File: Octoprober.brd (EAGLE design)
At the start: 130.8 x 91.7 mm, 144 parts, among them J1 10118193-0001LF, J2 26-60-4020, P1 TC33X-2-103E, SW1 101-0134-EV, SW2 EVQ-Q2203W, SW3 EVQ-Q2203W, SW4 EVQ-Q2203W, SW5 EVQ-Q2203W, U1 P8X32A-M44, U10 MAX31855KASA+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

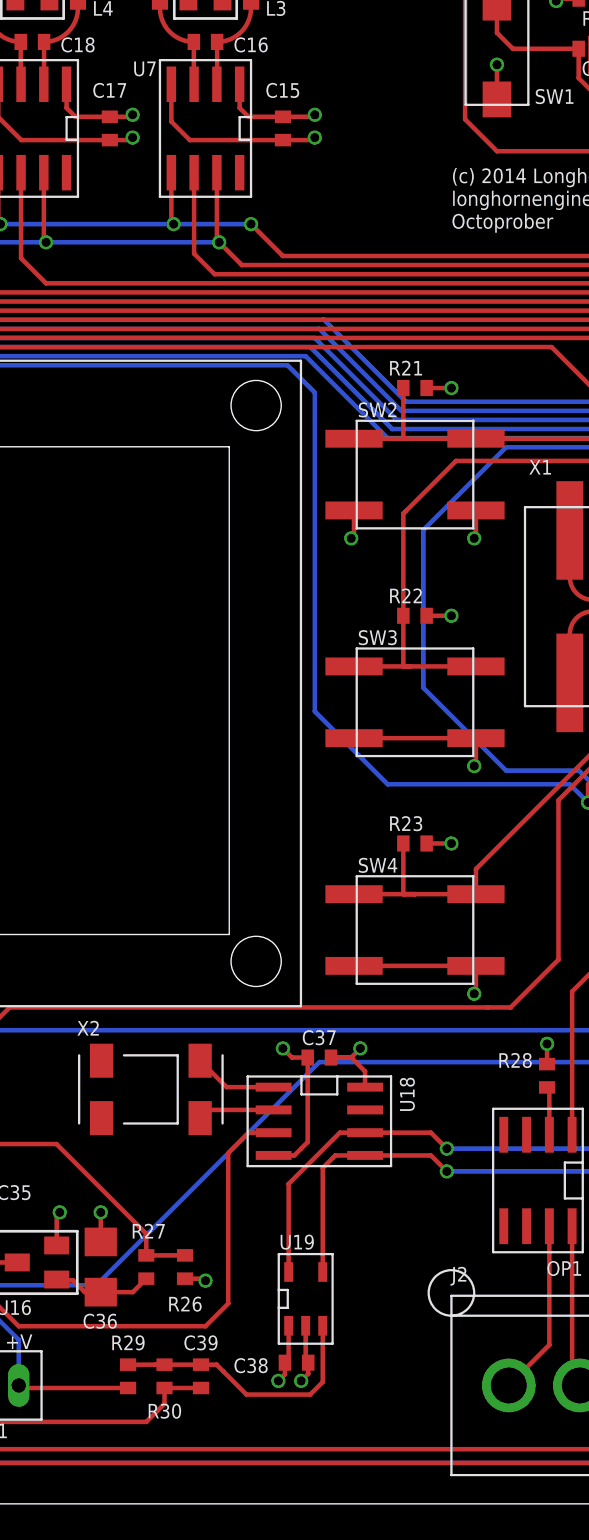
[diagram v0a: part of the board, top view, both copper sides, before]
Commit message: Evened out power traces on C17
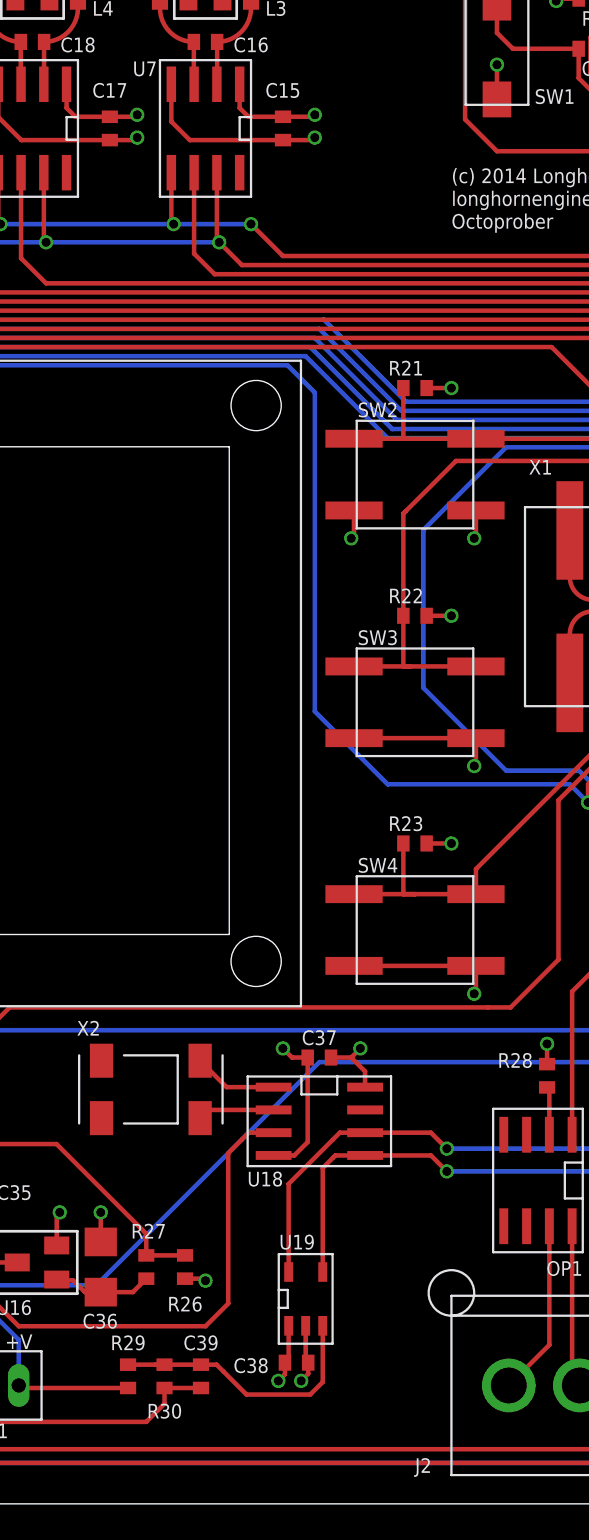
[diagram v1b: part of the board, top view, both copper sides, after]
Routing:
- net 3.3V: track 257.7 -> 256.8 mm
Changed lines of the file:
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@@
 </element>
 <element name="U$2" library="PP_Aesthetics" package="OCTOPROBER_LOGO" value="OCTOPROBER_LOGONORMAL" x="0.508" y="7.112"/>
-<element name="J2" library="PP_Connectors" package="MOLEX_KK_2" value="26-60-4020" x="101.854" y="6.604"/>
+<element name="J2" library="PP_Connectors" package="MOLEX_KK_2" value="26-60-4020" x="101.854" y="6.604" smashed="yes">
+<attribute name="NAME" x="94.742" y="1.7272" size="0.8128" layer="21" font="vector"/>
+</element>
 <element name="OP1" library="PP_DigitalIC" package="SOIC-8" value="ACPL-227" x="101.6" y="18.034" rot="R180"/>
 <element name="R28" library="PP_Passives" package="0402" value="120" x="102.108" y="23.876" smashed="yes" rot="R270">
@@
 <attribute name="NAME" x="15.748" y="87.738" size="0.8128" layer="21" font="vector"/>
 </element>
-<element name="U18" library="PP_DigitalIC" package="SOIC-8" value="DS1340Z-33+" x="89.408" y="21.336" rot="R270"/>
+<element name="U18" library="PP_DigitalIC" package="SOIC-8" value="DS1340Z-33+" x="89.408" y="21.336" smashed="yes" rot="R270">
+<attribute name="NAME" x="85.384" y="17.708" size="0.8128" layer="21" font="vector"/>
+</element>
 <element name="C37" library="PP_Passives" package="0402" value="0.1uF" x="89.408" y="24.892" smashed="yes" rot="R180">
 <attribute name="NAME" x="88.427" y="25.5905" size="0.8128" layer="25" font="vector"/>
@@
 <wire x1="49.53" y1="77.47" x2="59.436" y2="77.47" width="0.254" layer="2"/>
 <wire x1="59.436" y1="77.47" x2="69.342" y2="77.47" width="0.254" layer="2"/>
-<wire x1="69.342" y1="77.47" x2="78.994" y2="77.47" width="0.254" layer="2"/>
-<wire x1="78.994" y1="77.47" x2="89.154" y2="77.47" width="0.254" layer="2"/>
+<wire x1="69.342" y1="77.47" x2="79.248" y2="77.47" width="0.254" layer="2"/>
+<wire x1="79.248" y1="77.47" x2="89.154" y2="77.47" width="0.254" layer="2"/>
 <wire x1="27.178" y1="77.358" x2="28.59" y2="77.358" width="0.254" layer="1"/>
 <wire x1="28.59" y1="77.358" x2="28.702" y2="77.47" width="0.254" layer="1"/>
@@
 <wire x1="89.042" y1="77.358" x2="89.154" y2="77.47" width="0.254" layer="1"/>
 <via x="89.154" y="77.47" extent="1-16" drill="0.5"/>
-<wire x1="77.724" y1="77.358" x2="78.882" y2="77.358" width="0.254" layer="1"/>
-<wire x1="78.882" y1="77.358" x2="78.994" y2="77.47" width="0.254" layer="1"/>
-<via x="78.994" y="77.47" extent="1-16" drill="0.5"/>
+<wire x1="77.724" y1="77.358" x2="79.136" y2="77.358" width="0.254" layer="1"/>
+<wire x1="79.136" y1="77.358" x2="79.248" y2="77.47" width="0.254" layer="1"/>
+<via x="79.248" y="77.47" extent="1-16" drill="0.5"/>
 <wire x1="67.818" y1="77.358" x2="69.23" y2="77.358" width="0.254" layer="1"/>
 <wire x1="69.23" y1="77.358" x2="69.342" y2="77.47" width="0.254" layer="1"/>
@@
 <contactref element="U19" pad="2"/>
 <wire x1="88.758" y1="24.892" x2="88.758" y2="20.178" width="0.254" layer="1"/>
-<wire x1="88.758" y1="20.178" x2="88.392" y2="19.812" width="0.254" layer="1"/>
-<wire x1="88.392" y1="19.812" x2="88.011" y2="19.431" width="0.254" layer="1"/>
+<wire x1="88.758" y1="20.178" x2="88.011" y2="19.431" width="0.254" layer="1"/>
 <wire x1="88.011" y1="19.431" x2="86.858" y2="19.431" width="0.254" layer="1"/>
 <wire x1="88.758" y1="24.892" x2="87.884" y2="24.892" width="0.254" layer="1"/>
@@
 <wire x1="49.53" y1="76.2" x2="59.436" y2="76.2" width="0.254" layer="15"/>
 <wire x1="59.436" y1="76.2" x2="69.342" y2="76.2" width="0.254" layer="15"/>
-<wire x1="69.342" y1="76.2" x2="78.994" y2="76.2" width="0.254" layer="15"/>
-<wire x1="78.994" y1="76.2" x2="89.154" y2="76.2" width="0.254" layer="15"/>
+<wire x1="69.342" y1="76.2" x2="79.248" y2="76.2" width="0.254" layer="15"/>
+<wire x1="79.248" y1="76.2" x2="89.154" y2="76.2" width="0.254" layer="15"/>
 <wire x1="89.154" y1="76.2" x2="95.504" y2="76.2" width="0.254" layer="15"/>
 <wire x1="27.178" y1="76.058" x2="28.56" y2="76.058" width="0.254" layer="1"/>
@@
 <wire x1="69.2" y1="76.058" x2="69.342" y2="76.2" width="0.254" layer="1"/>
 <via x="69.342" y="76.2" extent="1-16" drill="0.5"/>
-<wire x1="77.724" y1="76.058" x2="78.852" y2="76.058" width="0.254" layer="1"/>
-<wire x1="78.852" y1="76.058" x2="78.994" y2="76.2" width="0.254" layer="1"/>
-<via x="78.994" y="76.2" extent="1-16" drill="0.5"/>
+<wire x1="77.724" y1="76.058" x2="79.106" y2="76.058" width="0.254" layer="1"/>
+<wire x1="79.106" y1="76.058" x2="79.248" y2="76.2" width="0.254" layer="1"/>
+<via x="79.248" y="76.2" extent="1-16" drill="0.5"/>
 <wire x1="87.376" y1="76.058" x2="89.012" y2="76.058" width="0.254" layer="1"/>
 <wire x1="89.012" y1="76.058" x2="89.154" y2="76.2" width="0.254" layer="1"/>
@@
 <wire x1="91.958" y1="23.241" x2="91.958" y2="24.12" width="0.254" layer="1"/>
 <wire x1="91.958" y1="24.12" x2="91.186" y2="24.892" width="0.254" layer="1"/>
-<wire x1="91.186" y1="24.892" x2="90.058" y2="24.892" width="0.254" layer="1"/>
 <wire x1="90.058" y1="24.892" x2="91.186" y2="24.892" width="0.254" layer="1"/>
 <wire x1="91.186" y1="24.892" x2="91.694" y2="25.4" width="0.254" layer="1"/>

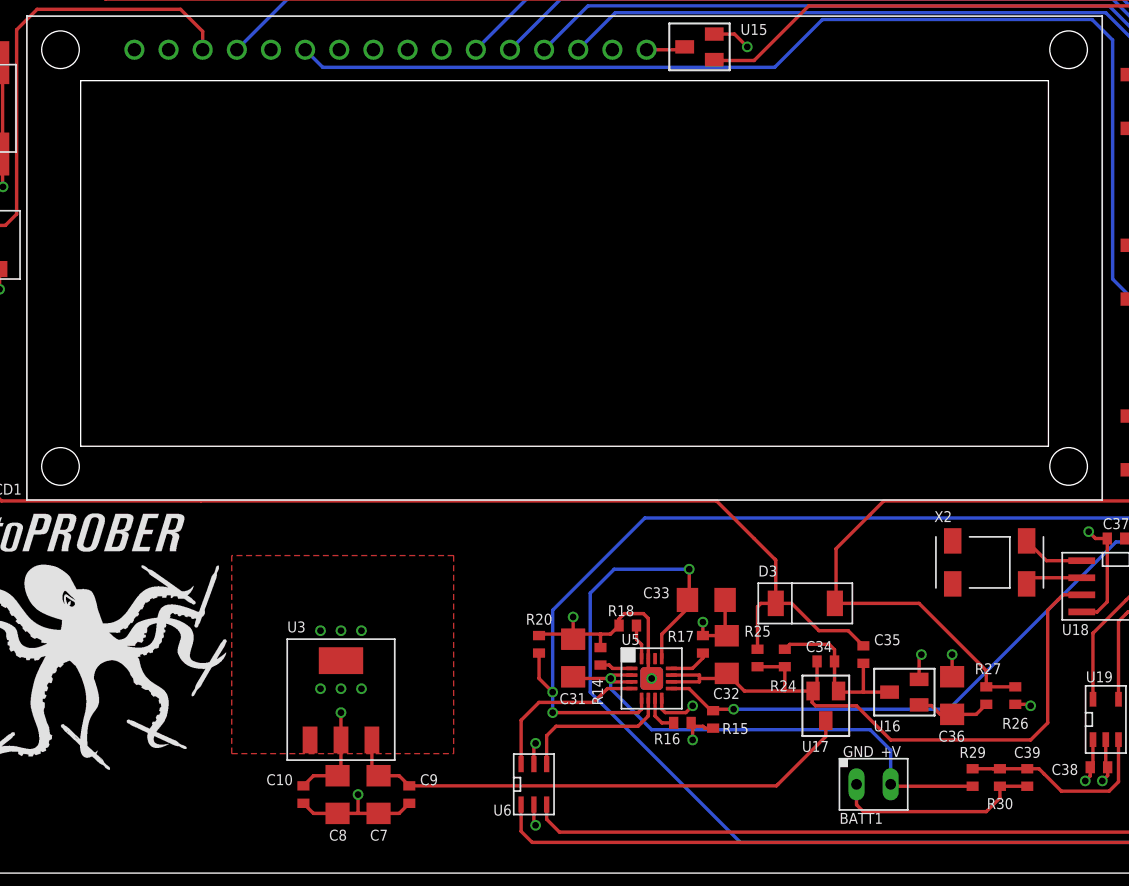
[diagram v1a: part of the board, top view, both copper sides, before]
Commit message: Changed footprint for Regulator
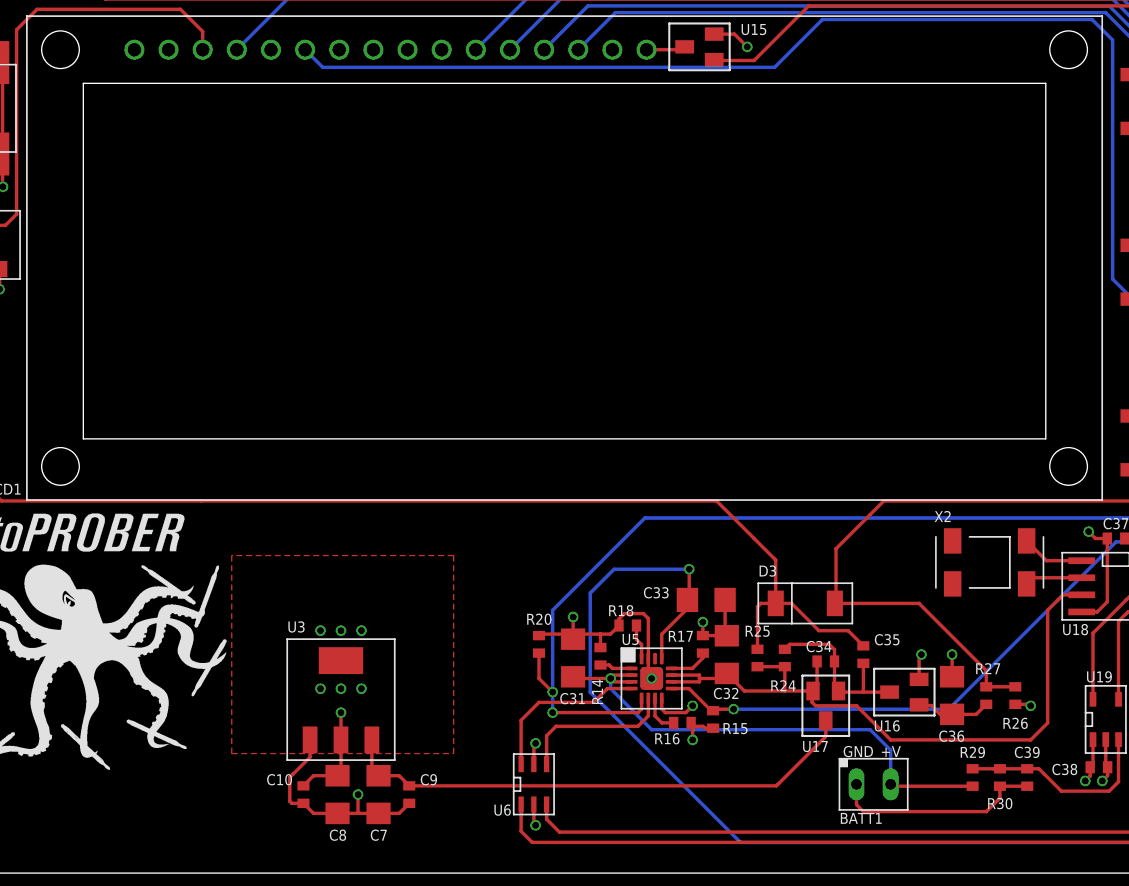
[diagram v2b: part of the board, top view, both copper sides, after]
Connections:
- net 3.3V: now also U3.COM2
- net GND: no longer U3.COM2
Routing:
- net GND: track 388.5 -> 394.7 mm, vias 57 -> 51
- net 3.3V: vias 28 -> 34
- added copper zone on layer 1, net 3.3V
- removed copper zone on layer 1, net GND
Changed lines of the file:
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@@
 <contactref element="C10" pad="2"/>
 <contactref element="C7" pad="2"/>
-<contactref element="U3" pad="COM2"/>
 <contactref element="U3" pad="IN"/>
 <contactref element="C8" pad="2"/>
@@
 <via x="74.93" y="16.256" extent="1-16" drill="0.5"/>
 <wire x1="74.93" y1="16.256" x2="74.93" y2="16.764" width="0.254" layer="2"/>
-<polygon width="0.254" layer="1">
-<vertex x="40.132" y="8.89"/>
-<vertex x="40.132" y="23.622"/>
-<vertex x="23.622" y="23.622"/>
-<vertex x="23.622" y="8.89"/>
-</polygon>
 <wire x1="28.956" y1="5.192" x2="29.706" y2="4.442" width="0.254" layer="1"/>
 <wire x1="29.706" y1="4.442" x2="31.496" y2="4.442" width="0.254" layer="1"/>
@@
 <wire x1="33.02" y1="5.842" x2="32.512" y2="5.842" width="0.254" layer="2"/>
 <wire x1="31.496" y1="4.442" x2="33.02" y2="4.442" width="0.254" layer="1"/>
-<via x="30.226" y="18.034" extent="1-16" drill="0.5"/>
-<via x="31.75" y="18.034" extent="1-16" drill="0.5"/>
-<via x="33.274" y="18.034" extent="1-16" drill="0.5"/>
-<via x="33.274" y="13.716" extent="1-16" drill="0.5"/>
-<via x="31.75" y="13.716" extent="1-16" drill="0.5"/>
-<via x="30.226" y="13.716" extent="1-16" drill="0.5"/>
 <wire x1="46.101" y1="5.104" x2="46.101" y2="3.683" width="0.254" layer="1"/>
 <wire x1="46.101" y1="3.683" x2="46.228" y2="3.556" width="0.254" layer="1"/>
@@
 <wire x1="88.392" y1="6.858" x2="87.884" y2="6.858" width="0.254" layer="2"/>
 <contactref element="LCD1" pad="1"/>
+<wire x1="29.45" y1="9.906" x2="29.45" y2="8.622" width="0.254" layer="1"/>
+<wire x1="29.45" y1="8.622" x2="28.194" y2="7.366" width="0.254" layer="1"/>
+<wire x1="28.194" y1="7.366" x2="27.94" y2="7.112" width="0.254" layer="1"/>
+<wire x1="27.94" y1="7.112" x2="27.94" y2="5.334" width="0.254" layer="1"/>
+<wire x1="27.94" y1="5.334" x2="28.082" y2="5.192" width="0.254" layer="1"/>
+<wire x1="28.082" y1="5.192" x2="28.956" y2="5.192" width="0.254" layer="1"/>
 </signal>
 <signal name="RES">
@@
 <via x="4.318" y="43.434" extent="1-16" drill="0.5"/>
 <wire x1="4.318" y1="43.434" x2="4.318" y2="42.926" width="0.254" layer="15"/>
+<contactref element="U3" pad="COM2"/>
+<polygon width="0.254" layer="1">
+<vertex x="40.132" y="8.89"/>
+<vertex x="40.132" y="23.622"/>
+<vertex x="23.622" y="23.622"/>
+<vertex x="23.622" y="8.89"/>
+</polygon>
+<via x="30.226" y="13.716" extent="1-16" drill="0.5"/>
+<via x="31.75" y="13.716" extent="1-16" drill="0.5"/>
+<via x="33.274" y="13.716" extent="1-16" drill="0.5"/>
+<via x="33.274" y="18.034" extent="1-16" drill="0.5"/>
+<via x="31.75" y="18.034" extent="1-16" drill="0.5"/>
+<via x="30.226" y="18.034" extent="1-16" drill="0.5"/>
 </signal>
 <signal name="SD_RW">

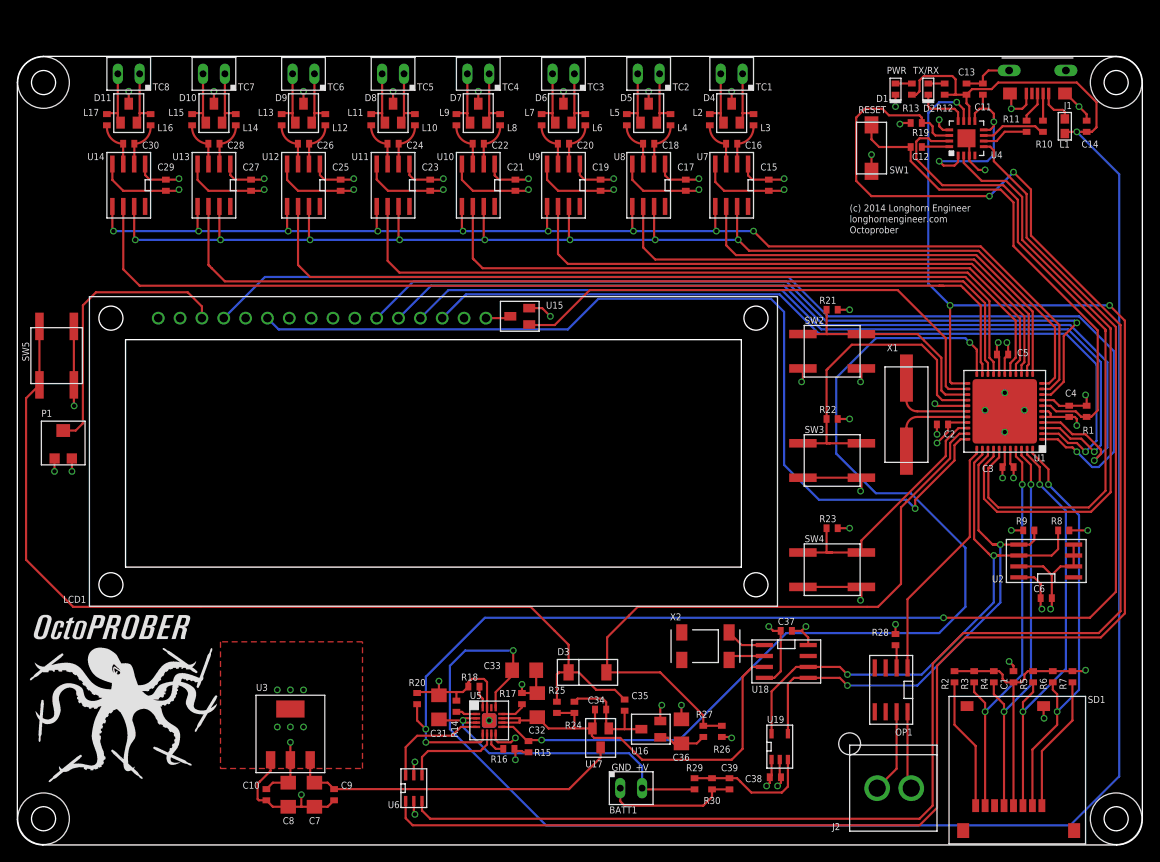
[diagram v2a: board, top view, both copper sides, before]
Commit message: Changed FT230X RST to be controlled by PROP
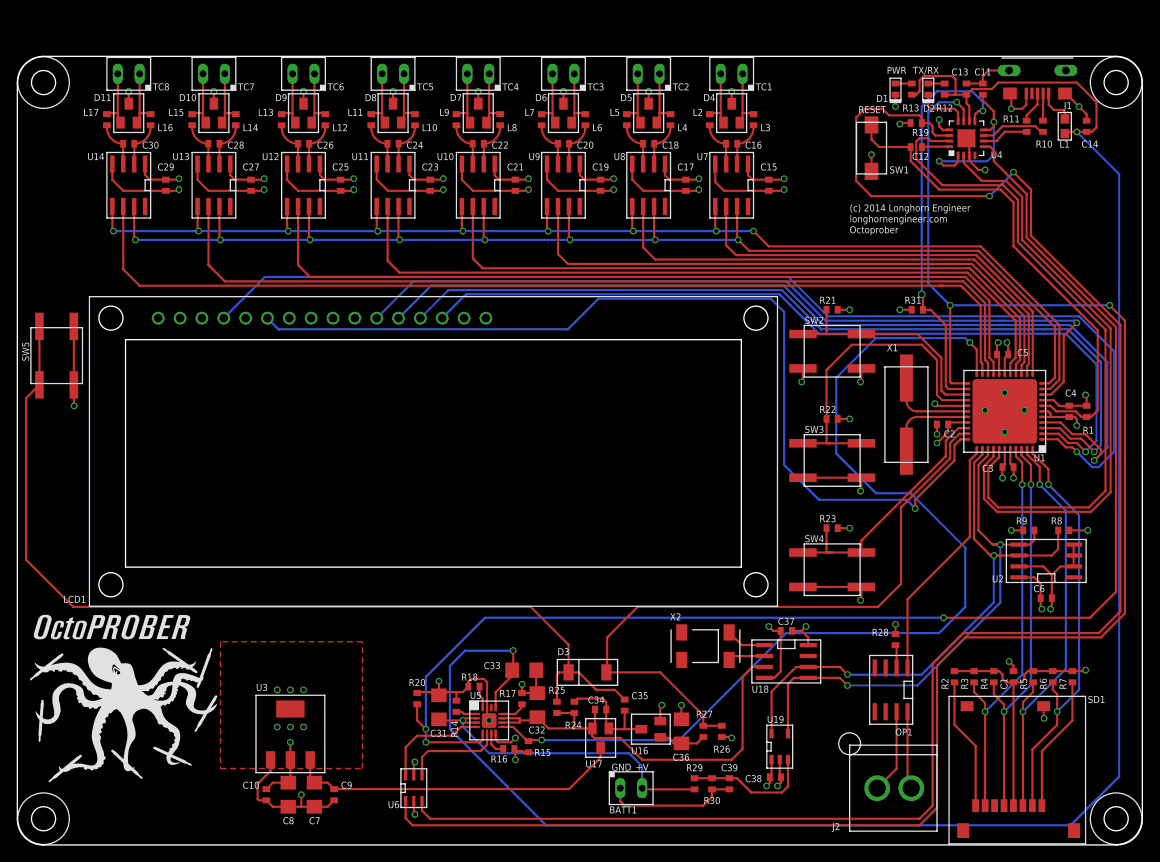
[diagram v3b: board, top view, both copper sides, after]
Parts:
- removed P1: TC33X-2-103E, PP_Passives:TC33_TRIMMER
- removed U15: PMV22EN,215, PP_DiscreteSemi:SOT-23
- added R31: 10K, PP_Passives:0402
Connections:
- removed net BK_GATE: U1.24, U15.1
- new net FT230_RST: R31.2, U1.24, U4.9
- net 3.3V: now also R31.1; no longer P1.1
- net 3V3OUT: no longer U4.9
- net BK_GND: no longer U15.3
- net CONTRAST: no longer P1.2
- net GND: no longer P1.3, U15.2
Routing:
- net BK_GATE: track 60.7 -> 0.00 mm
- net FT230_RST: track 0.00 -> 48.1 mm, vias 0 -> 2
- net CONTRAST: track 32.9 -> 0.00 mm
- net GND: track 394.7 -> 389.2 mm, vias 51 -> 49
- net BK_GND: track 3.05 -> 0.00 mm
- net 3V3OUT: track 21.8 -> 19.4 mm
